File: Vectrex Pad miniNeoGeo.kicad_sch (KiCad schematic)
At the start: 27 parts, among them J1 DB9_Female, SW1 SW_Push, SW2 SW_Push, SW3 SW_Push, SW4 SW_Push, SW5 SW_DP3T, SW6 SW_DP3T, U1 NE555D, U2 74LVC2G00, U3 74LVC2G32

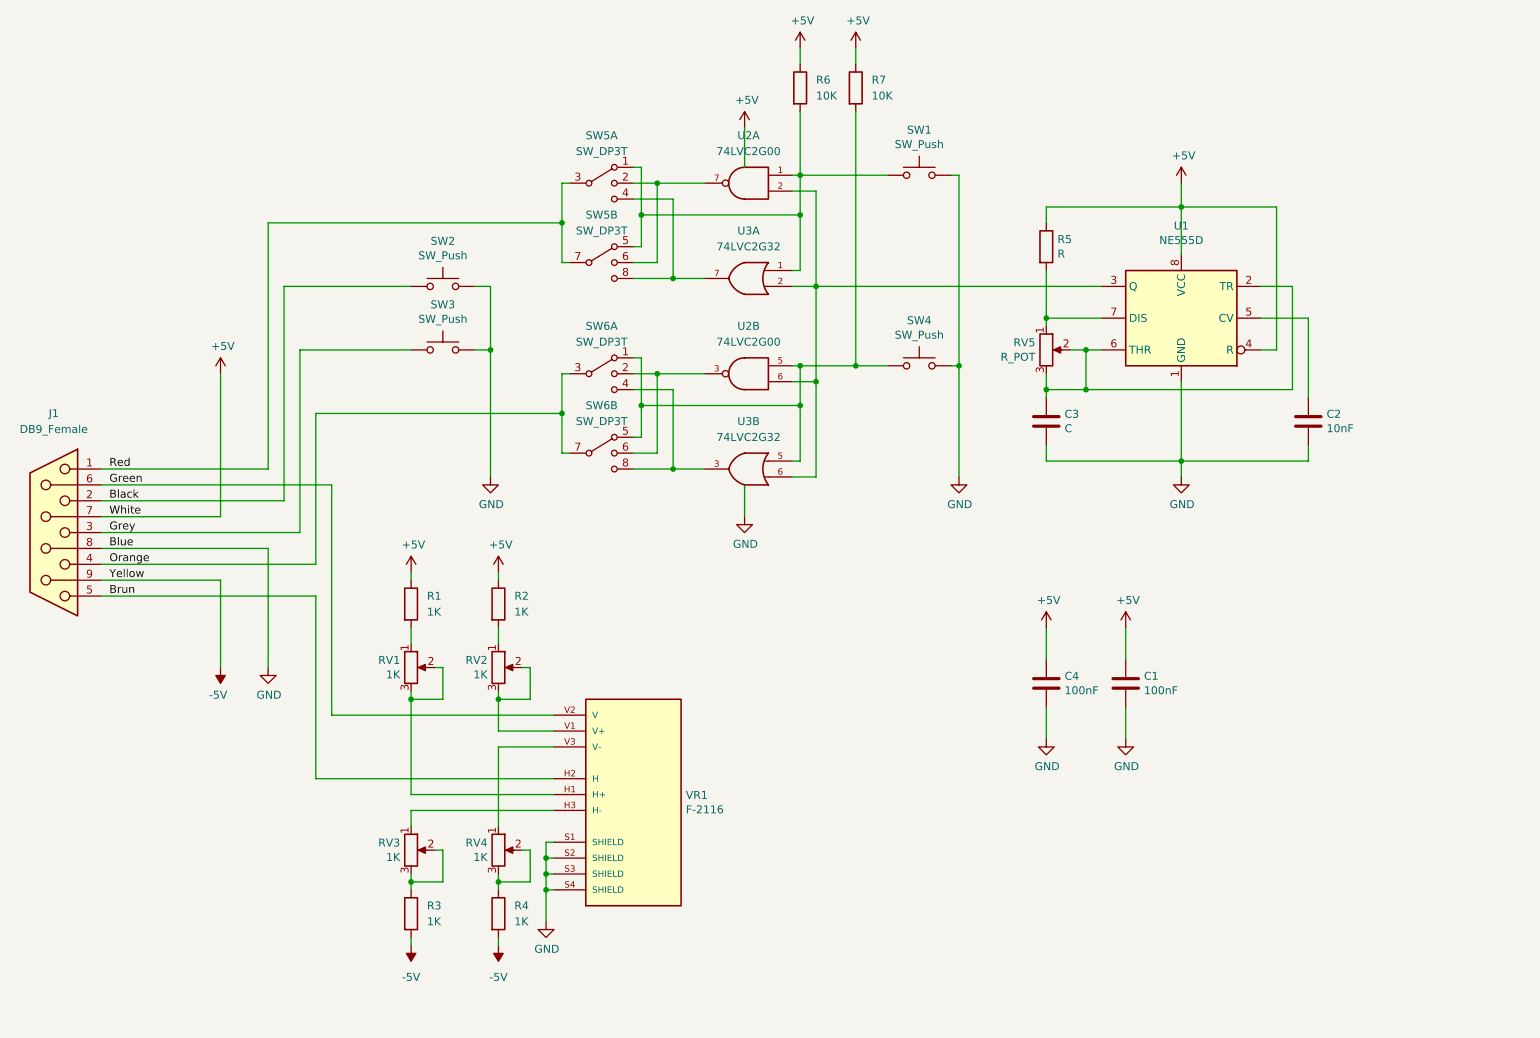
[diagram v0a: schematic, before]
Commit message: Production ready
Complete turn over of the board and passage of all the SMD components on the component side. To allow an assembly in factory.
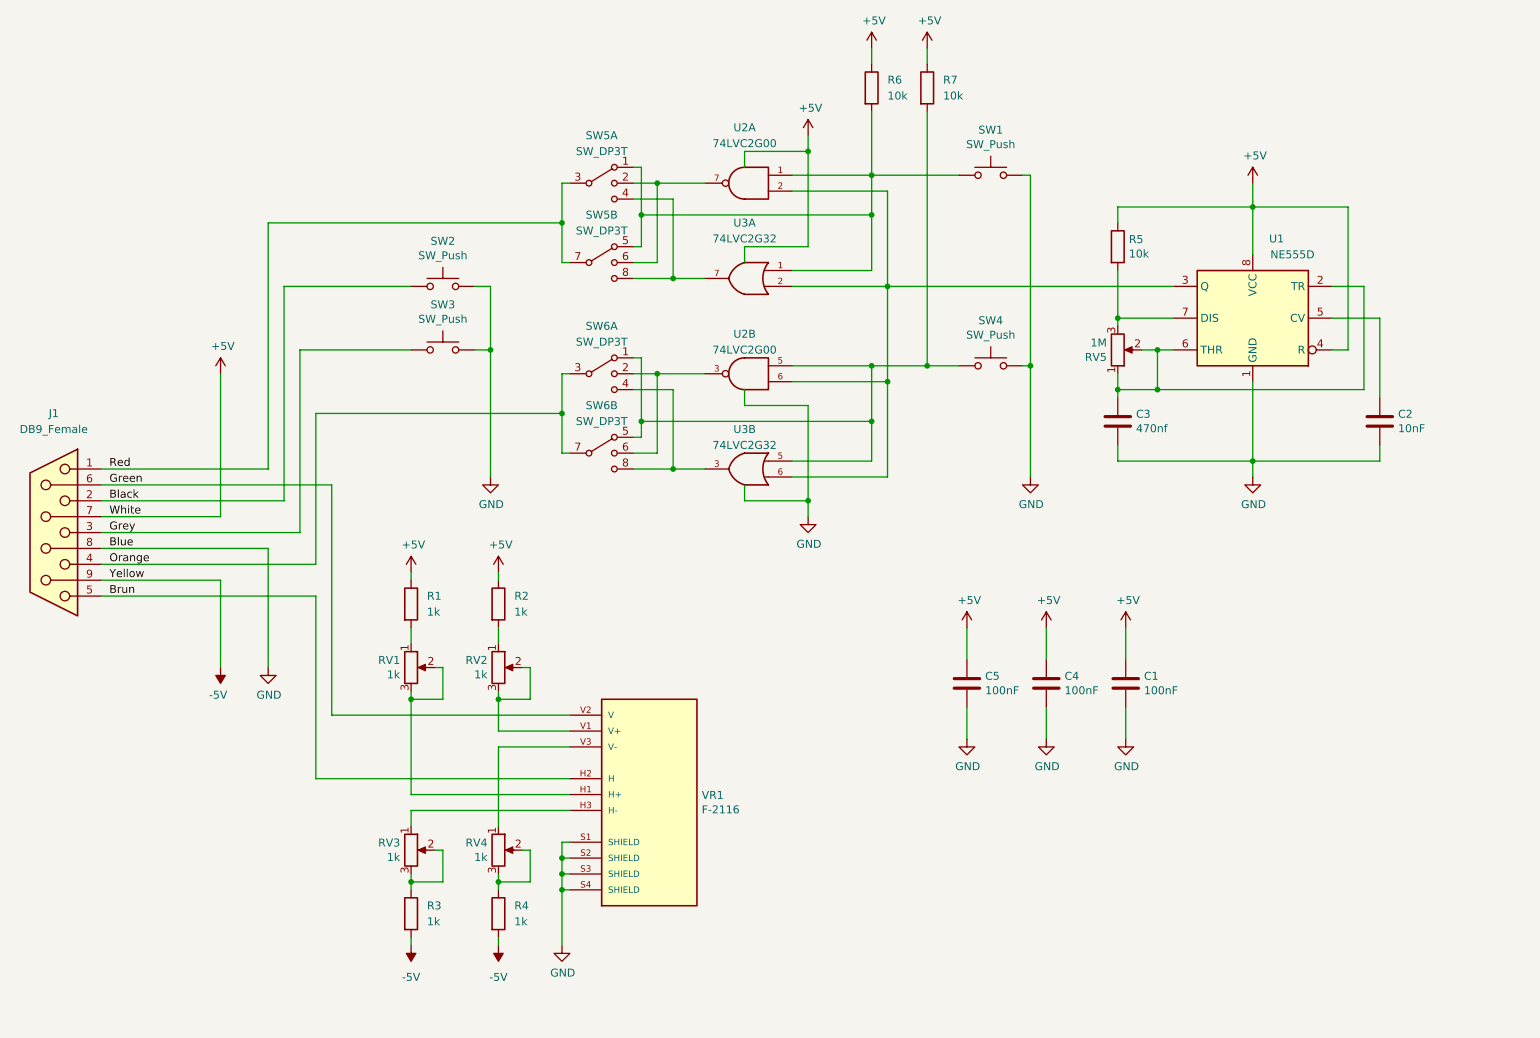
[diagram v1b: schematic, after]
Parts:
- added C5: 100nF, Capacitor_SMD:C_0805_2012Metric, symbol Device:C
- C3: value C -> 470nf
- R1, R2, R3, R4, RV1, RV2, RV3, RV4: value 1K -> 1k
- R5: value R -> 10k
- R6, R7: value 10K -> 10k
- RV5: value R_POT -> 1M
- U1: footprint Package_SO:SOIC-8_3.9x4.9mm_P1.27mm -> Package_SO:TSSOP-8_4.4x3mm_P0.65mm
- U2, U3: footprint Package_SO:SSOP-8_2.95x2.8mm_P0.65mm -> Vectrex Pad miniNeoGeo:SSOP-8_2.95x2.8mm_P0.65mm
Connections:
- net +5V: now also C5.1
- net GND: now also C5.2
- net at C3.1, RV5.2, U1.2 (TR)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: now also RV5.1; no longer RV5.3
- net at R5.2, U1.7 (DIS): now also RV5.3; no longer RV5.1
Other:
- title: (none) -> Vectrex Pad miniNeoGeo
- moved on the sheet: C2, C3, R5, R6, R7, RV5, SW1, SW4, U1, VR1

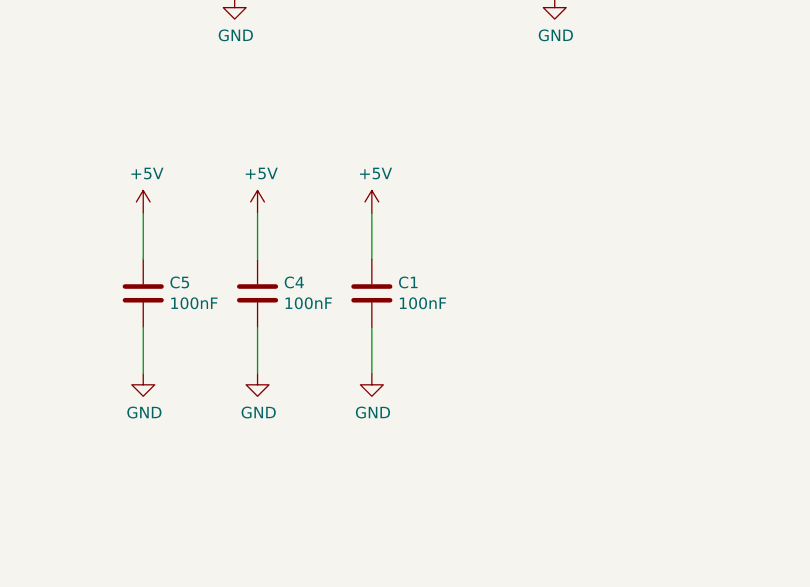
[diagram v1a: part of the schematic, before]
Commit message: Remove C1 & Cleaning
Remove C1 (Redundant with C4) and cleaning / optimizing trace & silkscreen
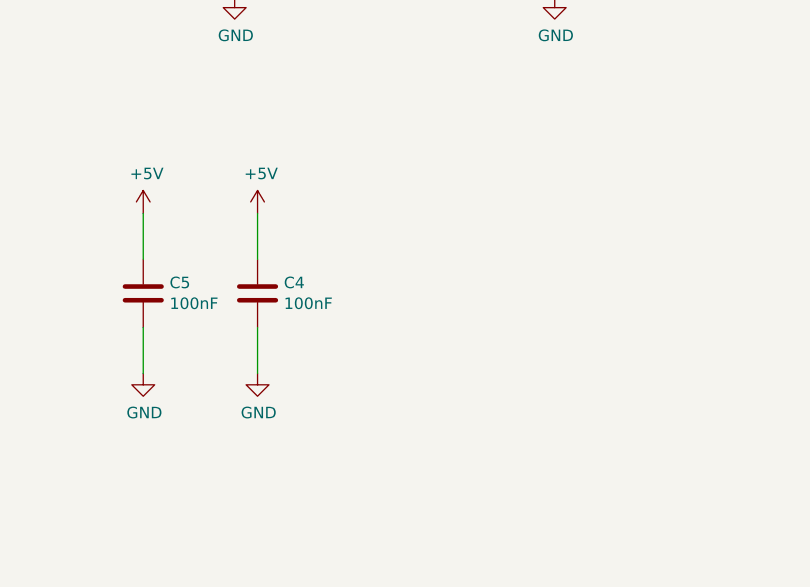
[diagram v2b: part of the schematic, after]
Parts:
- removed C1: 100nF, Capacitor_SMD:C_0805_2012Metric, symbol Device:C
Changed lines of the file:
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@@
-    (stroke (width 0) (type default) (color 0 0 0 0))
-  )
-  (wire (pts (xy 213.36 119.38) (xy 213.36 124.46))
     (stroke (width 0) (type default) (color 0 0 0 0))
   )
@@
   )
   (wire (pts (xy 102.87 154.94) (xy 104.14 154.94))
-    (stroke (width 0) (type default) (color 0 0 0 0))
-  )
-  (wire (pts (xy 213.36 132.08) (xy 213.36 137.16))
     (stroke (width 0) (type default) (color 0 0 0 0))
   )
@@
     (pin "1")
   )
-  (symbol (lib_id "power:+5V") (at 213.36 119.38 0) (unit 1)
-    (in_bom yes) (on_board yes)
-    (property "Reference" "#PWR0113" (id 0) (at 213.36 123.19 0)
-      (effects (font (size 1.27 1.27)) hide)
-    )
-    (property "Value" "+5V" (id 1) (at 213.741 114.9858 0))
-    (property "Footprint" "" (id 2) (at 213.36 119.38 0)
-      (effects (font (size 1.27 1.27)) hide)
-    )
-    (property "Datasheet" "" (id 3) (at 213.36 119.38 0)
-      (effects (font (size 1.27 1.27)) hide)
-    )
-    (pin "1")
-  )
   (symbol (lib_id "power:-5V") (at 113.03 170.18 180) (unit 1)
     (in_bom yes) (on_board yes) (fields_autoplaced)
@@
     )
     (pin "1")
-  )
-  (symbol (lib_id "Device:C") (at 213.36 128.27 0) (unit 1)
-    (in_bom yes) (on_board yes)
-    (property "Reference" "C1" (id 0) (at 216.281 127.1016 0)
-      (effects (font (size 1.27 1.27)) (justify left))
-    )
-    (property "Value" "100nF" (id 1) (at 216.281 129.413 0)
-      (effects (font (size 1.27 1.27)) (justify left))
-    )
-    (property "Footprint" "Capacitor_SMD:C_0805_2012Metric" (id 2) (at 214.3252 132.08 0)
-      (effects (font (size 1.27 1.27)) hide)
-    )
-    (property "Datasheet" "~" (id 3) (at 213.36 128.27 0)
-      (effects (font (size 1.27 1.27)) hide)
-    )
-    (pin "1")
-    (pin "2")
   )
   (symbol (lib_id "Connector:DB9_Female") (at 41.91 104.14 0) (mirror y) (unit 1)
@@
     (pin "2")
   )
-  (symbol (lib_id "power:GND") (at 213.36 137.16 0) (unit 1)
-    (in_bom yes) (on_board yes)
-    (property "Reference" "#PWR0116" (id 0) (at 213.36 143.51 0)
-      (effects (font (size 1.27 1.27)) hide)
-    )
-    (property "Value" "GND" (id 1) (at 213.487 141.5542 0))
-    (property "Footprint" "" (id 2) (at 213.36 137.16 0)
-      (effects (font (size 1.27 1.27)) hide)
-    )
-    (property "Datasheet" "" (id 3) (at 213.36 137.16 0)
-      (effects (font (size 1.27 1.27)) hide)
-    )
-    (pin "1")
-  )
   (symbol (lib_id "power:+5V") (at 200.66 119.38 0) (unit 1)
     (in_bom yes) (on_board yes)
@@
       (reference "#PWR0112") (unit 1) (value "GND") (footprint "")
     )
-    (path "/54204ad7-f595-4faa-bd26-1b82527580d4"
-      (reference "#PWR0113") (unit 1) (value "+5V") (footprint "")
-    )
     (path "/db0ee7aa-4fe7-4ee1-8d98-84ea7a305328"
       (reference "#PWR0114") (unit 1) (value "+5V") (footprint "")
@@
       (reference "#PWR0115") (unit 1) (value "GND") (footprint "")
     )
-    (path "/d18a3842-a5d5-42d0-977a-9a6580ae6aae"
-      (reference "#PWR0116") (unit 1) (value "GND") (footprint "")
-    )
     (path "/fdfa201b-6996-4bc7-8ff6-f3bf9d3b4290"
       (reference "#PWR0117") (unit 1) (value "+5V") (footprint "")
@@
       (reference "#PWR0122") (unit 1) (value "GND") (footprint "")
     )
-    (path "/cc06db85-8693-440f-97b0-0613299aa257"
-      (reference "C1") (unit 1) (value "100nF") (footprint "Capacitor_SMD:C_0805_2012Metric")
-    )
     (path "/00000000-0000-0000-0000-000061b5a283"

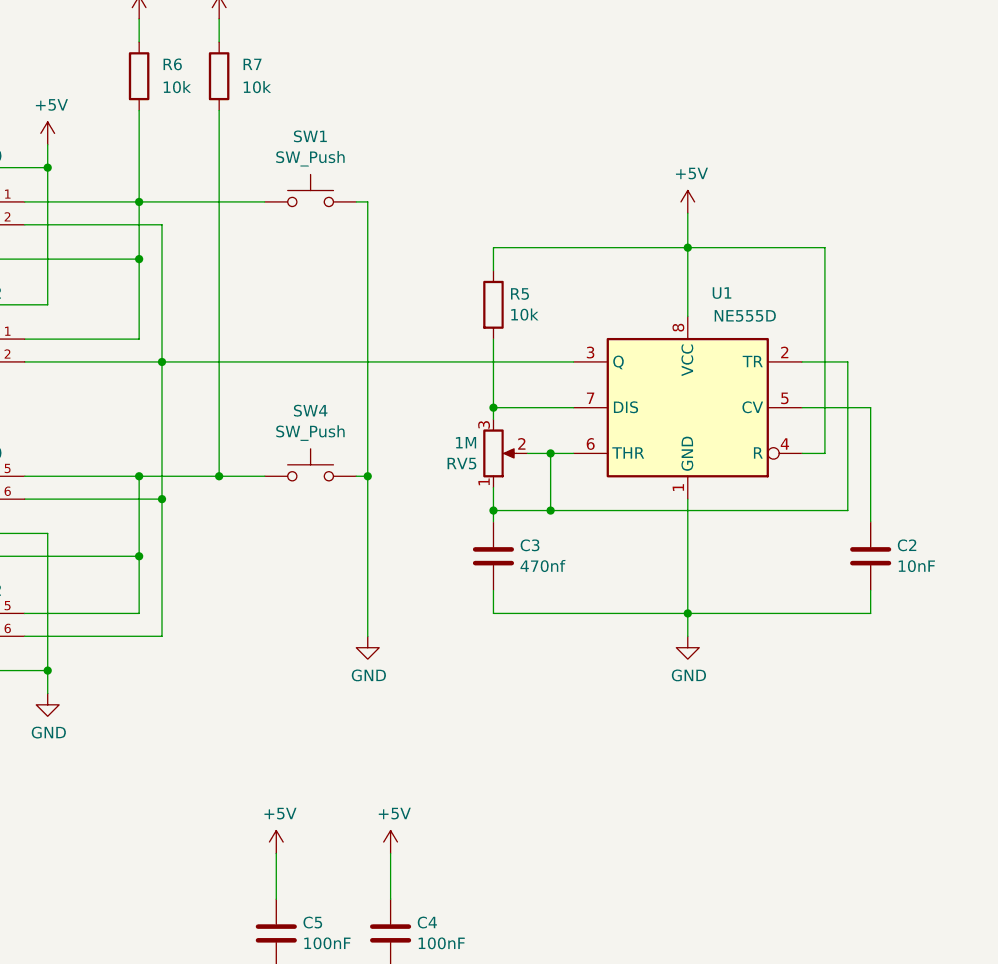
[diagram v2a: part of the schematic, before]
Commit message: Round track
Add Readme.md and PCB with round track.
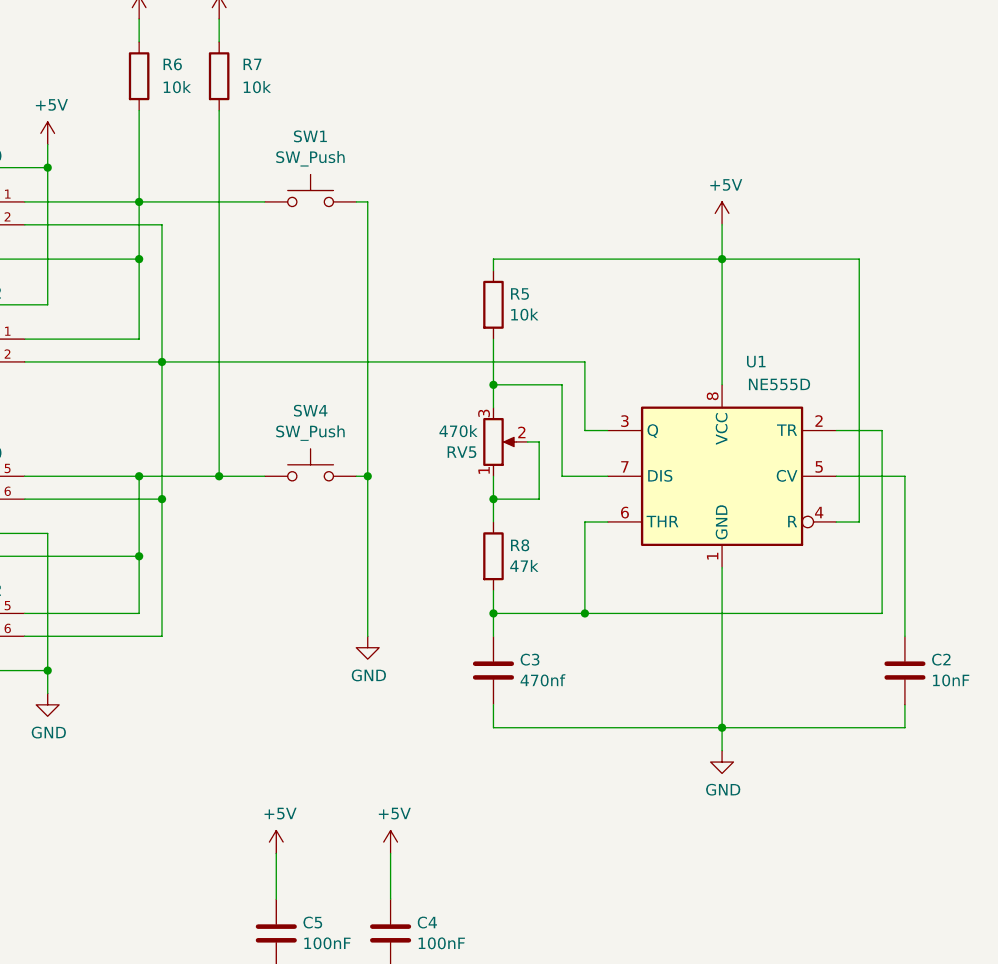
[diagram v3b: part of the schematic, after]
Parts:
- added R8: 47k, Resistor_SMD:R_0805_2012Metric, symbol Device:R
- RV5: value 1M -> 470k
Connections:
- net at C3.1, U1.2 (TR), U1.6 (THR): now also R8.2; no longer RV5.1, RV5.2
- new net: R8.1, RV5.1, RV5.2
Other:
- moved on the sheet: C2, C3, RV5, U1
